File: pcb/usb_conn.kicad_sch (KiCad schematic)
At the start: 10 parts, among them J2 CONN_USBC_RCPT_USB2.0_USB4085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, U6 IC_FTDI_FT231XS

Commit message: Added snubber DNP footprints and named nets on power page.
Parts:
- renumbered C21 to C50, C29 to C51, C30 to C52, C31 to C53, FB4 to FB5, R17 to R40, R24 to R41, R25 to R42, U6 to U8
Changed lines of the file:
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@@
   (symbol (lib_id "arjun_symbols:CH_GND") (at 58.42 127 0) (unit 1)
     (in_bom yes) (on_board yes)
-    (property "Reference" "#PWR046" (id 0) (at 58.42 132.08 0)
+    (property "Reference" "#PWR079" (id 0) (at 58.42 132.08 0)
       (effects (font (size 1.27 1.27)) hide)
     )
@@
   (symbol (lib_id ".arjun:CAP_CER_0u1_50V_X7R_0603") (at 96.52 60.96 0) (unit 1)
     (in_bom yes) (on_board yes)
-    (property "Reference" "C30" (id 0) (at 99.568 61.976 0)
+    (property "Reference" "C52" (id 0) (at 99.568 61.976 0)
       (effects (font (size 1.27 1.27)) (justify left))
     )
@@
   (symbol (lib_id "arjun_symbols:RES_5K11_1P_1{slash}10W_0603") (at 88.9 81.28 0) (unit 1)
     (in_bom yes) (on_board yes)
-    (property "Reference" "R25" (id 0) (at 85.725 85.09 90)
+    (property "Reference" "R42" (id 0) (at 85.725 85.09 90)
       (effects (font (size 1.27 1.27)) (justify top))
     )
@@
   (symbol (lib_id "arjun_symbols:RES_0R_1{slash}8W_0805") (at 48.26 137.16 270) (unit 1)
     (in_bom yes) (on_board yes)
-    (property "Reference" "R17" (id 0) (at 44.45 133.985 90)
+    (property "Reference" "R40" (id 0) (at 44.45 133.985 90)
       (effects (font (size 1.27 1.27)) (justify top))
     )
@@
   (symbol (lib_id "power:GND") (at 73.66 68.58 0) (unit 1)
     (in_bom yes) (on_board yes)
-    (property "Reference" "#PWR059" (id 0) (at 73.66 74.93 0)
+    (property "Reference" "#PWR081" (id 0) (at 73.66 74.93 0)
       (effects (font (size 1.27 1.27)) hide)
     )
@@
   (symbol (lib_id "power:GND") (at 83.82 93.98 0) (unit 1)
     (in_bom yes) (on_board yes)
-    (property "Reference" "#PWR055" (id 0) (at 83.82 100.33 0)
+    (property "Reference" "#PWR082" (id 0) (at 83.82 100.33 0)
       (effects (font (size 1.27 1.27)) hide)
     )
@@
   (symbol (lib_id ".arjun:CAP_CER_0u01_50V_X7R_0603") (at 73.66 60.96 0) (unit 1)
     (in_bom yes) (on_board yes)
-    (property "Reference" "C29" (id 0) (at 76.708 61.976 0)
+    (property "Reference" "C51" (id 0) (at 76.708 61.976 0)
       (effects (font (size 1.27 1.27)) (justify left))
     )
@@
   (symbol (lib_id "arjun_symbols:CAP_CER_4700p_250V_X7R_0805") (at 40.64 147.32 90) (unit 1)
     (in_bom no) (on_board no)
-    (property "Reference" "C21" (id 0) (at 45.72 143.51 90)
+    (property "Reference" "C50" (id 0) (at 45.72 143.51 90)
       (effects (font (size 1.27 1.27)) (justify left))
     )
@@
   (symbol (lib_id ".arjun:FER_33R_6A_0603") (at 83.82 58.42 0) (unit 1)
     (in_bom yes) (on_board yes)
-    (property "Reference" "FB4" (id 0) (at 87.63 54.61 0))
+    (property "Reference" "FB5" (id 0) (at 87.63 54.61 0))
     (property "Value" "FER_33R_6A_0603" (id 1) (at 113.665 52.07 0)
       (effects (font (size 1.27 1.27)) hide)
@@
   (symbol (lib_id "power:+5V") (at 106.68 55.88 0) (unit 1)
     (in_bom yes) (on_board yes)
-    (property "Reference" "#PWR058" (id 0) (at 106.68 59.69 0)
+    (property "Reference" "#PWR083" (id 0) (at 106.68 59.69 0)
       (effects (font (size 1.27 1.27)) hide)
     )
@@
   (symbol (lib_id "power:GND") (at 33.02 149.86 0) (unit 1)
     (in_bom yes) (on_board yes)
-    (property "Reference" "#PWR043" (id 0) (at 33.02 156.21 0)
+    (property "Reference" "#PWR077" (id 0) (at 33.02 156.21 0)
       (effects (font (size 1.27 1.27)) hide)
     )
@@
   (symbol (lib_id ".arjun:CAP_CER_4u7_50V_X5R_0805") (at 106.68 60.96 0) (unit 1)
     (in_bom yes) (on_board yes)
-    (property "Reference" "C31" (id 0) (at 109.728 61.976 0)
+    (property "Reference" "C53" (id 0) (at 109.728 61.976 0)
       (effects (font (size 1.27 1.27)) (justify left))
     )
@@
   (symbol (lib_id "power:GND") (at 106.68 73.66 0) (unit 1)
     (in_bom yes) (on_board yes)
-    (property "Reference" "#PWR060" (id 0) (at 106.68 80.01 0)
+    (property "Reference" "#PWR084" (id 0) (at 106.68 80.01 0)
       (effects (font (size 1.27 1.27)) hide)
     )
@@
   (symbol (lib_id "arjun_symbols:RES_5K11_1P_1{slash}10W_0603") (at 78.74 81.28 0) (unit 1)
     (in_bom yes) (on_board yes)
-    (property "Reference" "R24" (id 0) (at 75.565 85.09 90)
+    (property "Reference" "R41" (id 0) (at 75.565 85.09 90)
       (effects (font (size 1.27 1.27)) (justify top))
     )
@@
   (symbol (lib_id "power:GND") (at 63.5 114.3 0) (unit 1)
     (in_bom yes) (on_board yes)
-    (property "Reference" "#PWR047" (id 0) (at 63.5 120.65 0)
+    (property "Reference" "#PWR080" (id 0) (at 63.5 120.65 0)
       (effects (font (size 1.27 1.27)) hide)
     )
@@
   (symbol (lib_id "arjun_symbols:IC_FTDI_FT231XS") (at 170.18 81.28 0) (unit 1)
     (in_bom yes) (on_board yes)
-    (property "Reference" "U6" (id 0) (at 173.99 76.2 0)
+    (property "Reference" "U8" (id 0) (at 173.99 76.2 0)
       (effects (font (size 1.27 1.27)) (justify left))
     )
@@
   (symbol (lib_id "arjun_symbols:CH_GND") (at 55.88 149.86 0) (unit 1)
     (in_bom yes) (on_board yes)
-    (property "Reference" "#PWR044" (id 0) (at 55.88 154.94 0)
-      (effects (font (size 1.27 1.27)) hide)
-    )
+    (property "Reference" "#PWR078" (id 0) (at 55.88 154.94 0)
+      (effects (font (size 1.27 1.27)) hide)
+    )

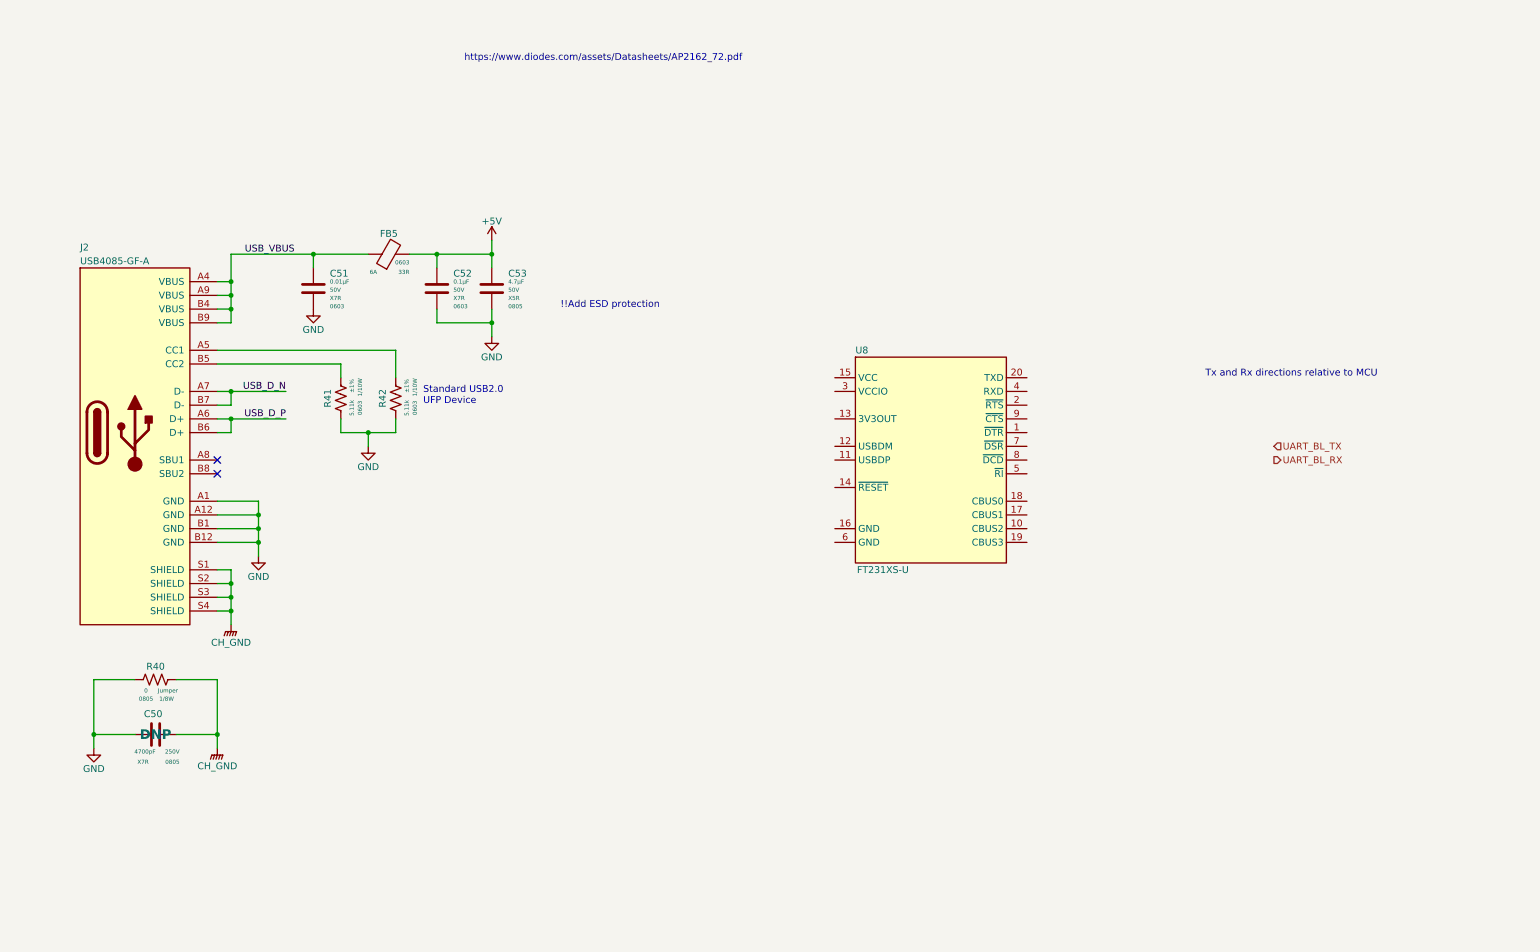
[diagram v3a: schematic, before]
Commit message: Updated ftdi page
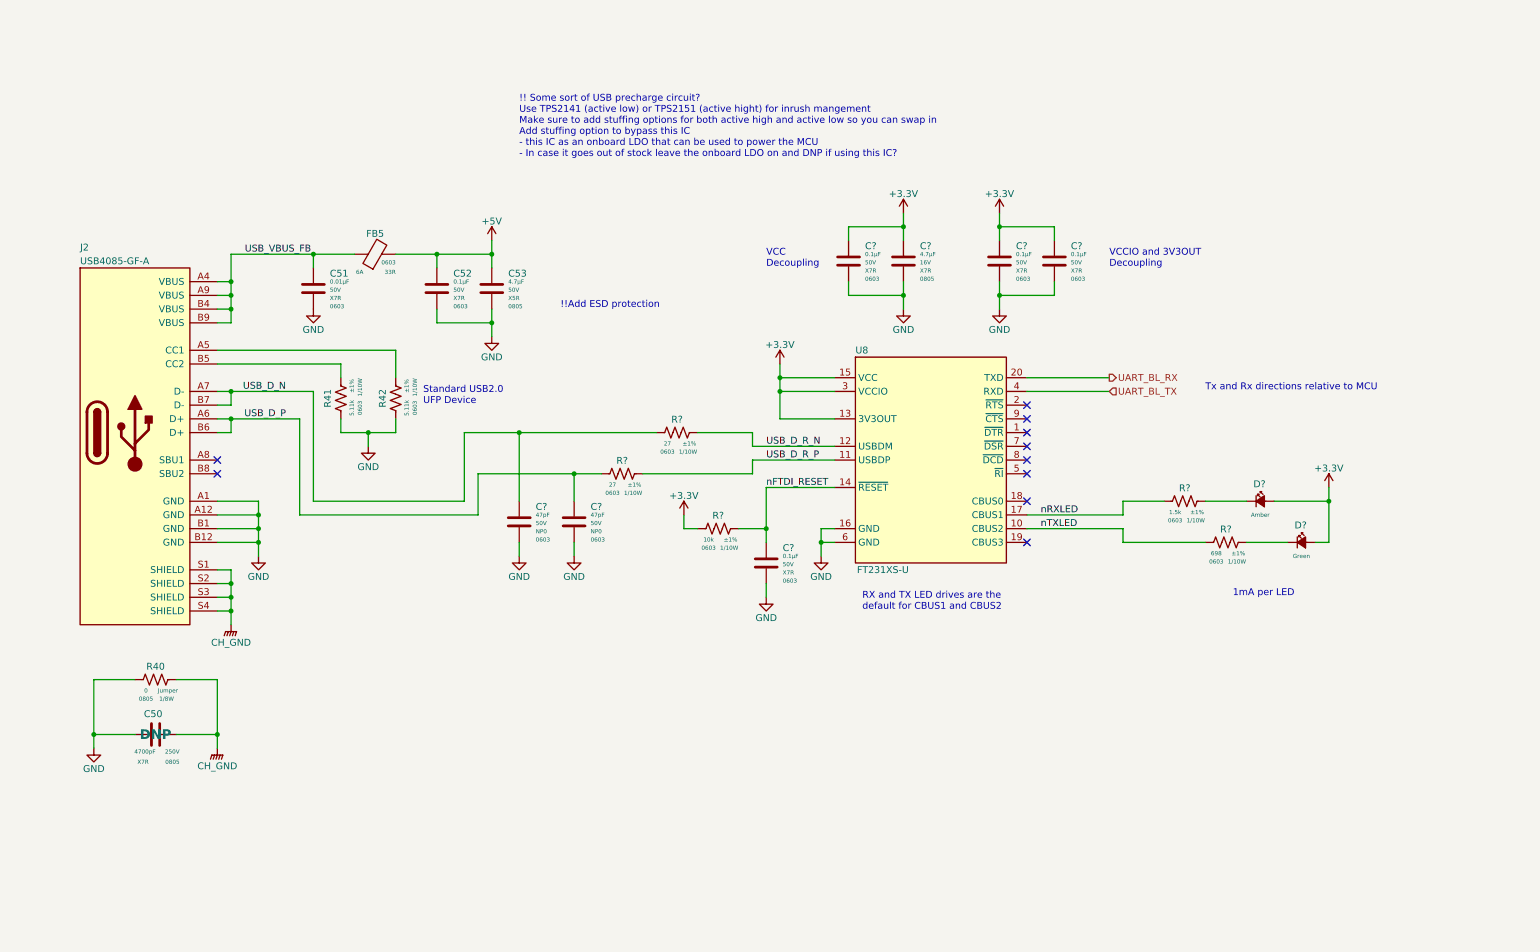
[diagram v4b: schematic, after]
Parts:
- added C? (x2): CAP_CER_47p_50V_NP0_0603, Capacitor_SMD:C_0603_1608Metric, symbol .arjun:CAP_CER_47p_50V_NP0_0603
- added C?: CAP_CER_4u7_16V_X7R_0805, Capacitor_SMD:C_0805_2012Metric, symbol .arjun:CAP_CER_4u7_16V_X7R_0805
- added C? (x4): CAP_CER_0u1_50V_X7R_0603, Capacitor_SMD:C_0603_1608Metric, symbol .arjun:CAP_CER_0u1_50V_X7R_0603
- added D?: LED_GREEN_0603, LED_SMD:LED_0603_1608Metric, symbol .arjun:LED_GREEN_0603
- added D?: LED_AMBER_0603, LED_SMD:LED_0603_1608Metric, symbol .arjun:LED_AMBER_0603
- added R? (x2): RES_27R_1P_1/10W_0603, Resistor_SMD:R_0603_1608Metric, symbol .arjun:RES_27R_1P_1/10W_0603
- added R?: RES_698R_1P_1/10W_0603, Resistor_SMD:R_0603_1608Metric, symbol .arjun:RES_698R_1P_1/10W_0603
- added R?: RES_10K_1P_1/10W_0603, Resistor_SMD:R_0603_1608Metric, symbol .arjun:RES_10K_1P_1/10W_0603
- added R?: RES_1K5_1P_1/10W_0603, Resistor_SMD:R_0603_1608Metric, symbol .arjun:RES_1K5_1P_1/10W_0603
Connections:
- net GND: now also U8.16 (GND), U8.6 (GND), C?.2, C?.2, C?.2, C?.2, C?.2, C?.2, C?.2
- net UART_BL_RX: now also U8.20 (TXD)
- net UART_BL_TX: now also U8.4 (RXD)
- net USB_D_N: now also C?.1, R?.2
- net USB_D_P: now also C?.1, R?.2
- net nTXLED: now reaches U8.10 (CBUS2)
- net nTXLED: now also R?.2
- net USB_D_R_P: now reaches U8.11 (USBDP)
- net USB_D_R_P: now also R?.1
- net USB_D_R_N: now reaches U8.12 (USBDM)
- net USB_D_R_N: now also R?.1
- net +3.3V: now reaches U8.13 (3V3OUT)
- net +3.3V: now also U8.15 (VCC), U8.3 (VCCIO), C?.1, C?.1, C?.1, C?.1, D?.2 (A), D?.2 (A), R?.2
- net nFTDI_RESET: now reaches U8.14 (~{RESET})
- net nFTDI_RESET: now also C?.1, R?.1
- net nRXLED: now reaches U8.17 (CBUS1)
- net nRXLED: now also R?.2
- net USB_VBUS renamed USB_VBUS_FB
- new net: D?.1 (K), R?.1 (x2)
- no-connect marks 2 -> 10
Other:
- note added: "!! Some sort of USB precharge circuit? Use TPS2141 (active low) or TPS2151 (active hight) for inrush mangement Make sure to add stuffing options for both active high and active low so you can swap in Add stuffing option to bypass this IC - this IC as an onboard LDO that can be used to power the MCU - In case it goes out of stock leave the onboard LDO on and DNP if using this IC?"
- note added: "1mA per LED"
- note added: "RX and TX LED drives are the default for CBUS1 and CBUS2"
- note added: "VCC Decoupling"
- note added: "VCCIO and 3V3OUT Decoupling"
- note removed: "https://www.diodes.com/assets/Datasheets/AP2162_72.pdf"
- moved on the sheet: FB5

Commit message: Added load switch to input to limit inrush
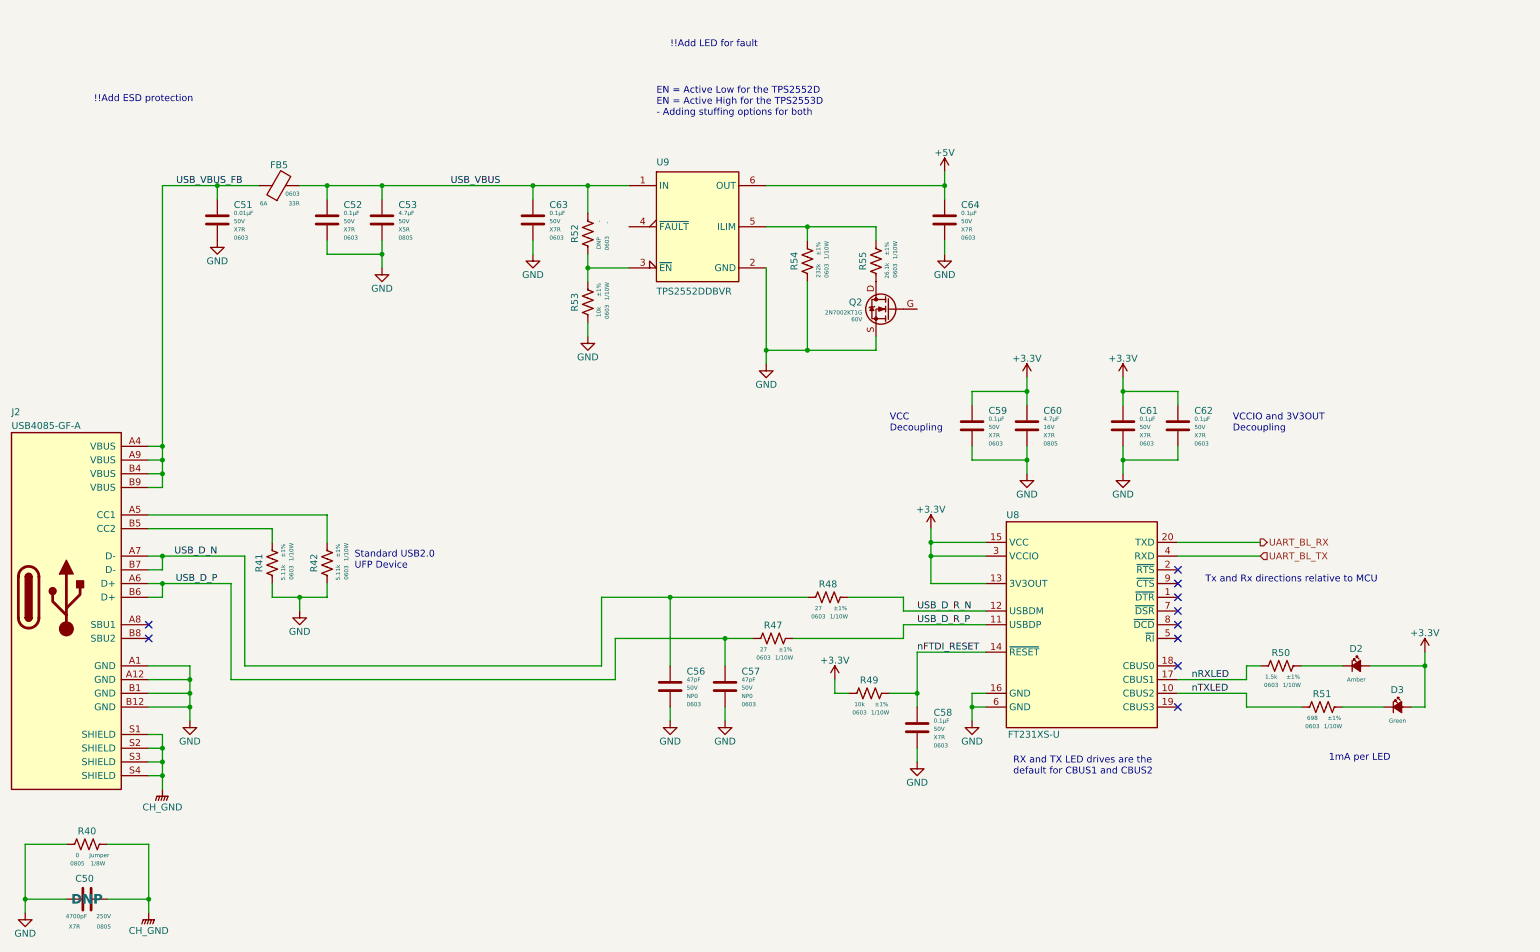
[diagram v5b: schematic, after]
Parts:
- added C63, C64: CAP_CER_0u1_50V_X7R_0603, Capacitor_SMD:C_0603_1608Metric, symbol .arjun:CAP_CER_0u1_50V_X7R_0603
- added Q2: NFET_60V_0A5_2N7002KT1G, arjun_footprints:SOT-23_ONSEMI, symbol .arjun:NFET_60V_0A5_2N7002KT1G
- added R52: RES_DNP_0603, Resistor_SMD:R_0603_1608Metric, symbol .arjun:RES_DNP_0603
- added R53: RES_10K_1P_1/10W_0603, Resistor_SMD:R_0603_1608Metric, symbol .arjun:RES_10K_1P_1/10W_0603
- added R54: RES_232K_1P_1/10W_0603, Resistor_SMD:R_0603_1608Metric, symbol .arjun:RES_232K_1P_1/10W_0603
- added R55: RES_26K1_1P_1/10W_0603, Resistor_SMD:R_0603_1608Metric, symbol .arjun:RES_26K1_1P_1/10W_0603
- added U9: IC_LSW_TI_TPS2552D, arjun_footprints:SOT-23-6_TI, symbol .arjun:IC_LSW_TI_TPS2552D
- gave numbers to parts that had none: 14
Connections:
- net +5V: now also C64.1, U9.6 (OUT); no longer C52.1, C53.1, FB5.2
- net GND: now also C63.2, C64.2, Q2.S, R53.2, R54.2, U9.2 (GND)
- new net: R52.2, R53.1, U9.3 (~{EN})
- new net: R54.1, R55.1, U9.5 (ILIM)
- new net: Q2.D, R55.2
- new net USB_VBUS: C52.1, C53.1, C63.1, FB5.2, R52.1, U9.1 (IN)
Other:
- note added: "!!Add LED for fault"
- note added: "EN = Active Low for the TPS2552D EN = Active High for the TPS2553D - Adding stuffing options for both"
- note removed: "!! Some sort of USB precharge circuit? Use TPS2141 (active low) or TPS2151 (active hight) for inrush mangement Make sure to add stuffing options for both active high and active low so you can swap in Add stuffing option to bypass this IC - this IC as an onboard LDO that can be used to power the MCU - In case it goes out of stock leave the onboard LDO on and DNP if using this IC?"
- moved on the sheet: C50, C51, C52, C53, C56, C57, C58, C59, C60, C61, C62, D2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

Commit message: Added load swtich current limit change FET and plumbed out signals to top level
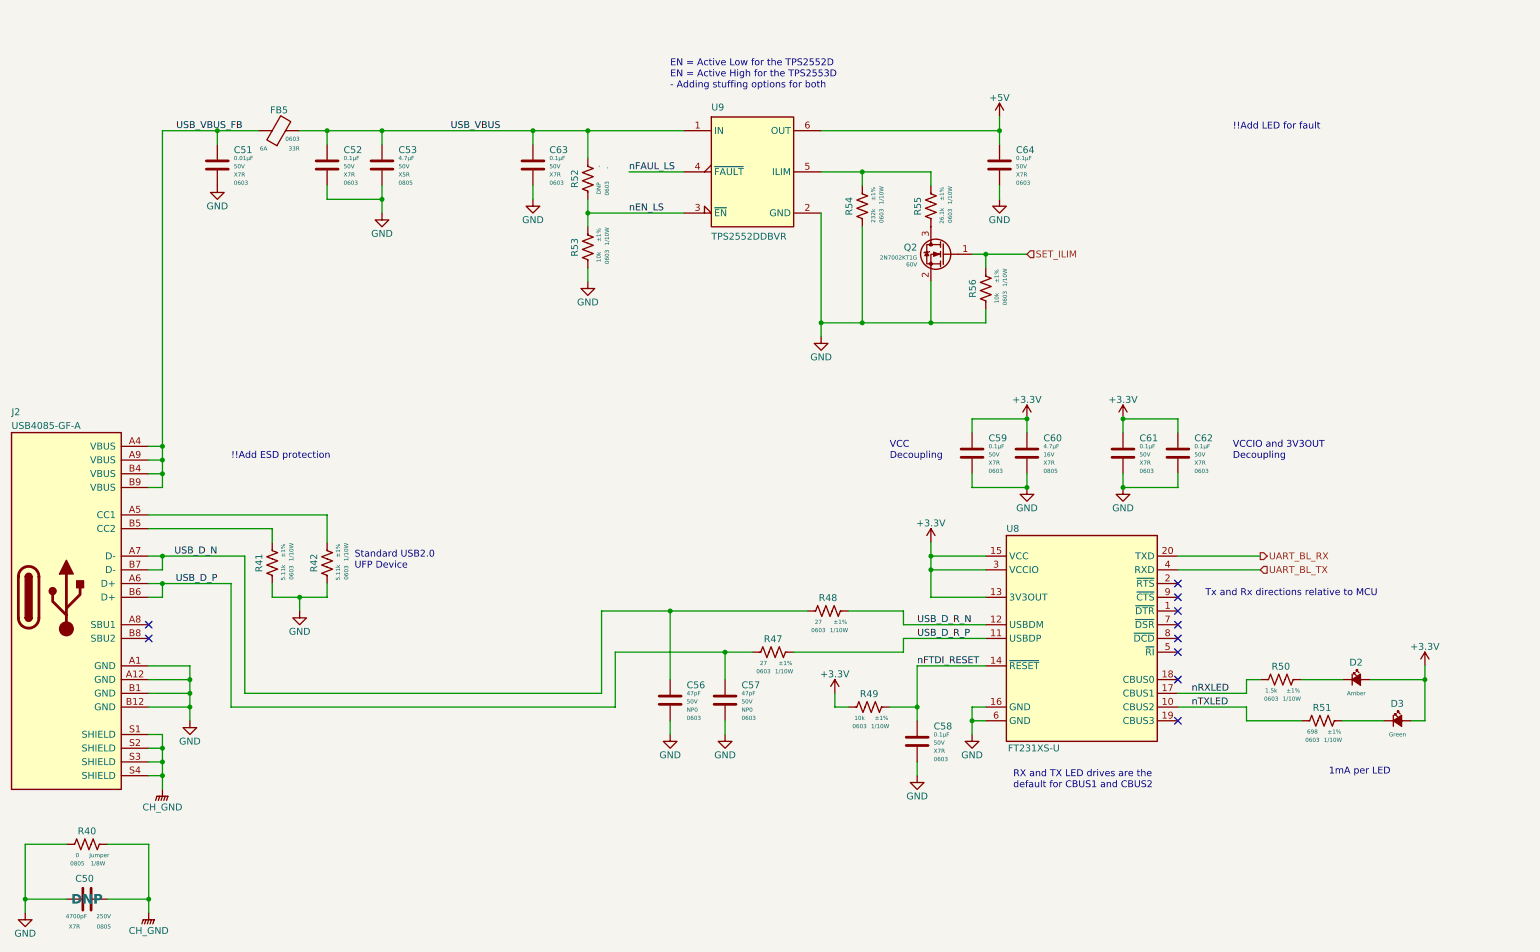
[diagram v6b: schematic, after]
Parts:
- added R56: RES_10K_1P_1/10W_0603, Resistor_SMD:R_0603_1608Metric, symbol .arjun:RES_10K_1P_1/10W_0603
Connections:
- net GND: now also Q2.2 (S), R56.2; no longer Q2.S
- net nEN_LS: now reaches R52.2, R53.1, U9.3 (~{EN})
- net nFAUL_LS: now reaches U9.4 (~{FAULT})
- net at R55.2: now also Q2.3 (D); no longer Q2.D
- new net SET_ILIM: Q2.1 (G), R56.1
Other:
- moved on the sheet: C51, C52, C53, C56, C57, C58, C59, C60, C61, C62, C63, C64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
